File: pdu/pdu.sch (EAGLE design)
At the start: 18 parts, among them IC1 FDN359BN, IC2 FDN359BN, IC3 FDN359BN

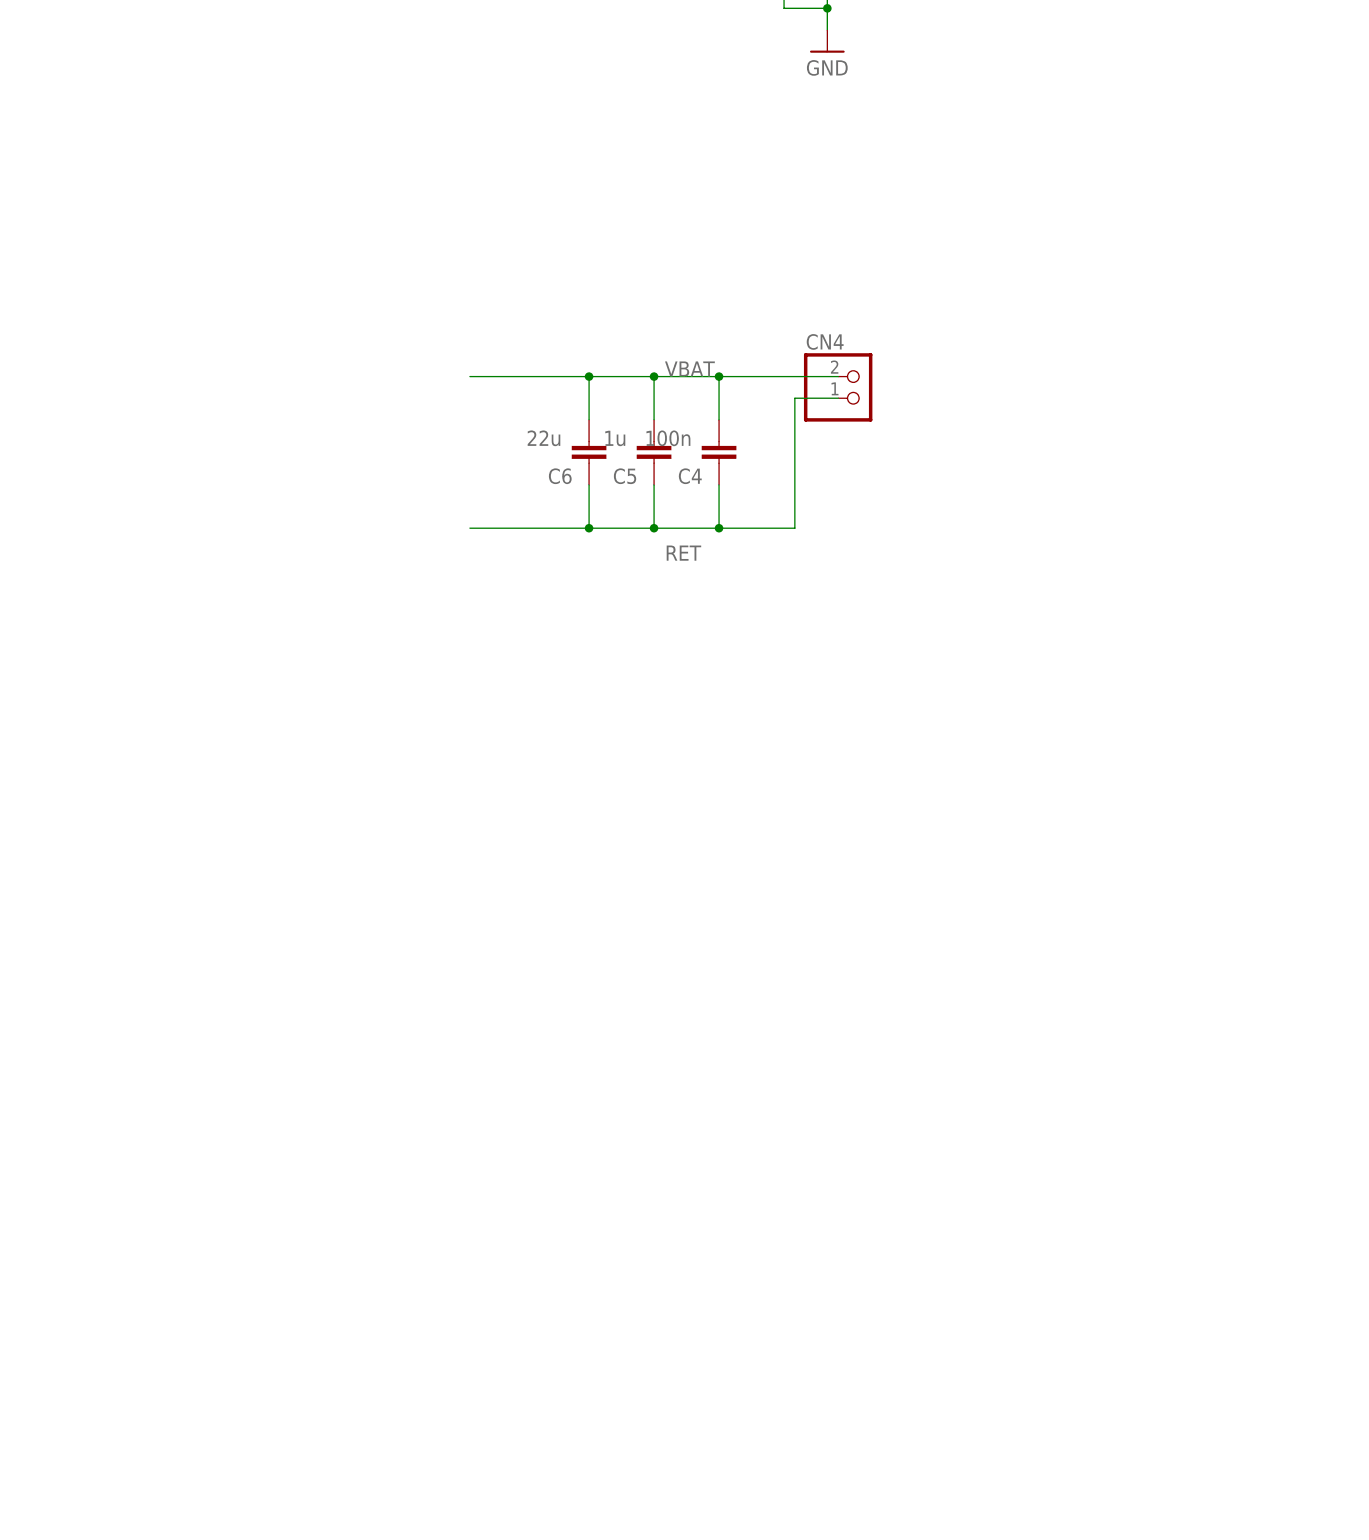
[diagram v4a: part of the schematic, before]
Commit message: fill length with conns
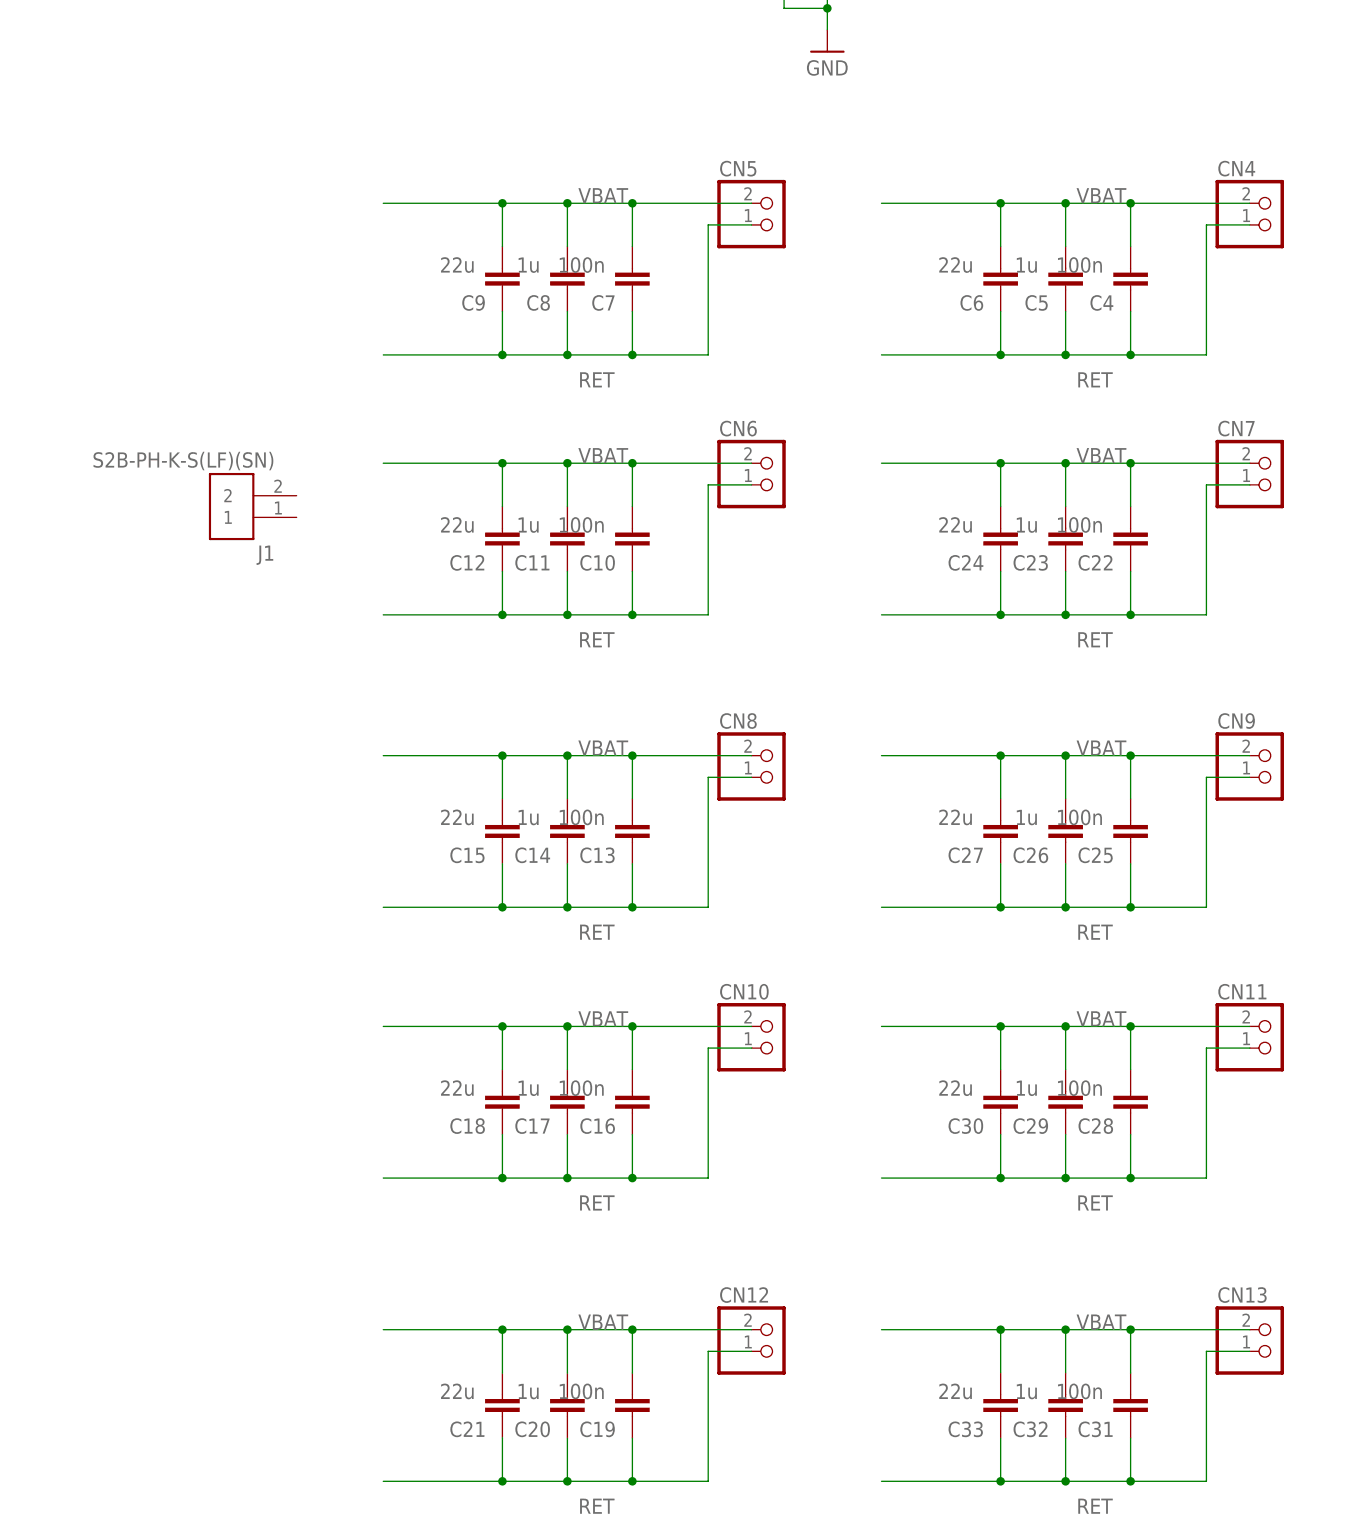
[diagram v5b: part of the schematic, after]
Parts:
- added C10, C13, C16, C19, C22, C25, C28, C31, C7: 100n, Capacitor:C_CHIP-0603(1608-METRIC)
- added C11, C14, C17, C20, C23, C26, C29, C32, C8: 1u, Capacitor:C_CHIP-0603(1608-METRIC)
- added C12, C15, C18, C21, C24, C27, C30, C33, C9: 22u, Capacitor:C_CHIP-0603(1608-METRIC)
- added CN10, CN11, CN12, CN13, CN5, CN6, CN7, CN8, CN9: (no value), adafruit:JST_2PIN-THM-RA
- added J1: S2B-PH-K-S(LF)(SN), Connectors:S2B-PH-K-S(LF)(SN)
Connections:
- net RET: now also C10.1, C11.1, C12.1, C13.1, C14.1, C15.1, C16.1, C17.1, C18.1, C19.1, C20.1, C21.1, C22.1, C23.1, C24.1, C25.1, C26.1, C27.1, C28.1, C29.1, C30.1, C31.1, C32.1, C33.1, C7.1, C8.1, C9.1, CN10.2, CN11.2, CN12.2, CN13.2, CN5.2, CN6.2, CN7.2, CN8.2, CN9.2
- net VBAT: now also C10.2, C11.2, C12.2, C13.2, C14.2, C15.2, C16.2, C17.2, C18.2, C19.2, C20.2, C21.2, C22.2, C23.2, C24.2, C25.2, C26.2, C27.2, C28.2, C29.2, C30.2, C31.2, C32.2, C33.2, C7.2, C8.2, C9.2, CN10.1, CN11.1, CN12.1, CN13.1, CN5.1, CN6.1, CN7.1, CN8.1, CN9.1
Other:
- moved on the sheet: C4, C5, C6, CN4

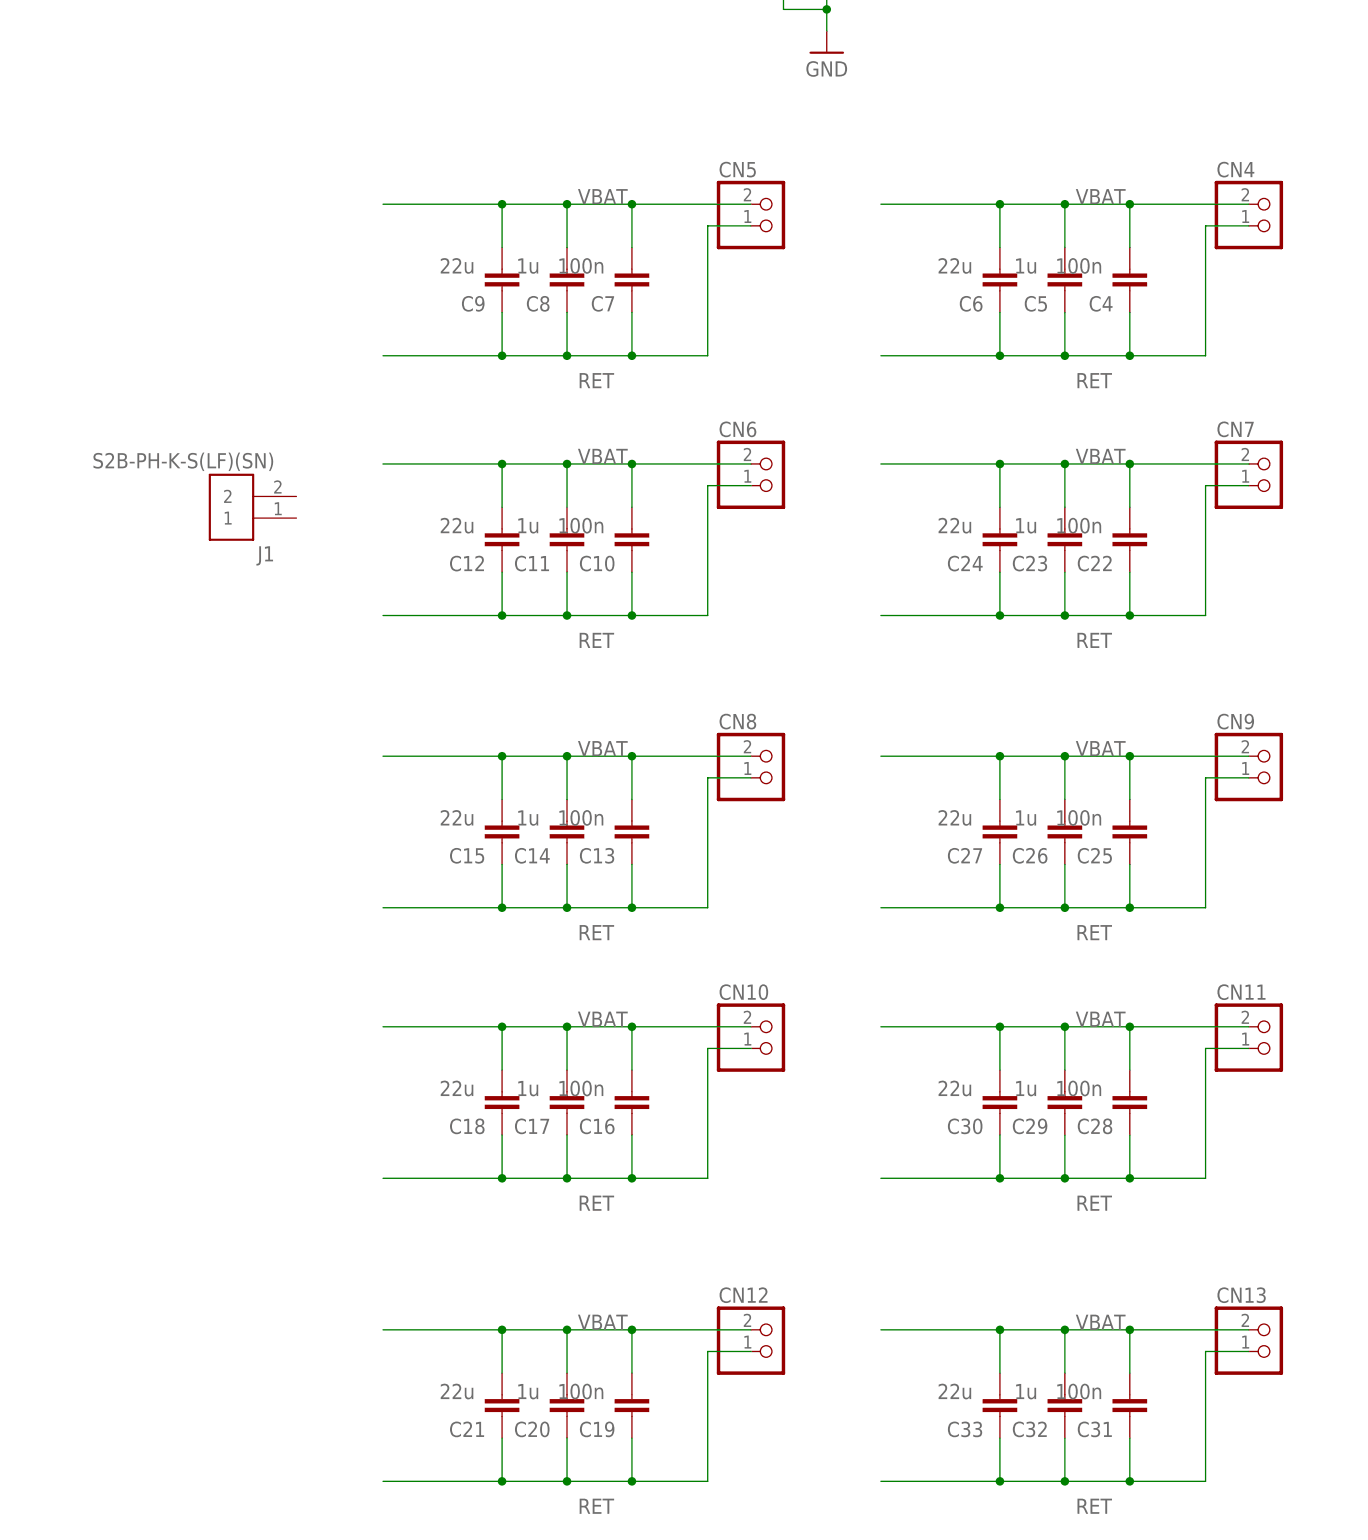
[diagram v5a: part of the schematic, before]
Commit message: swap connector
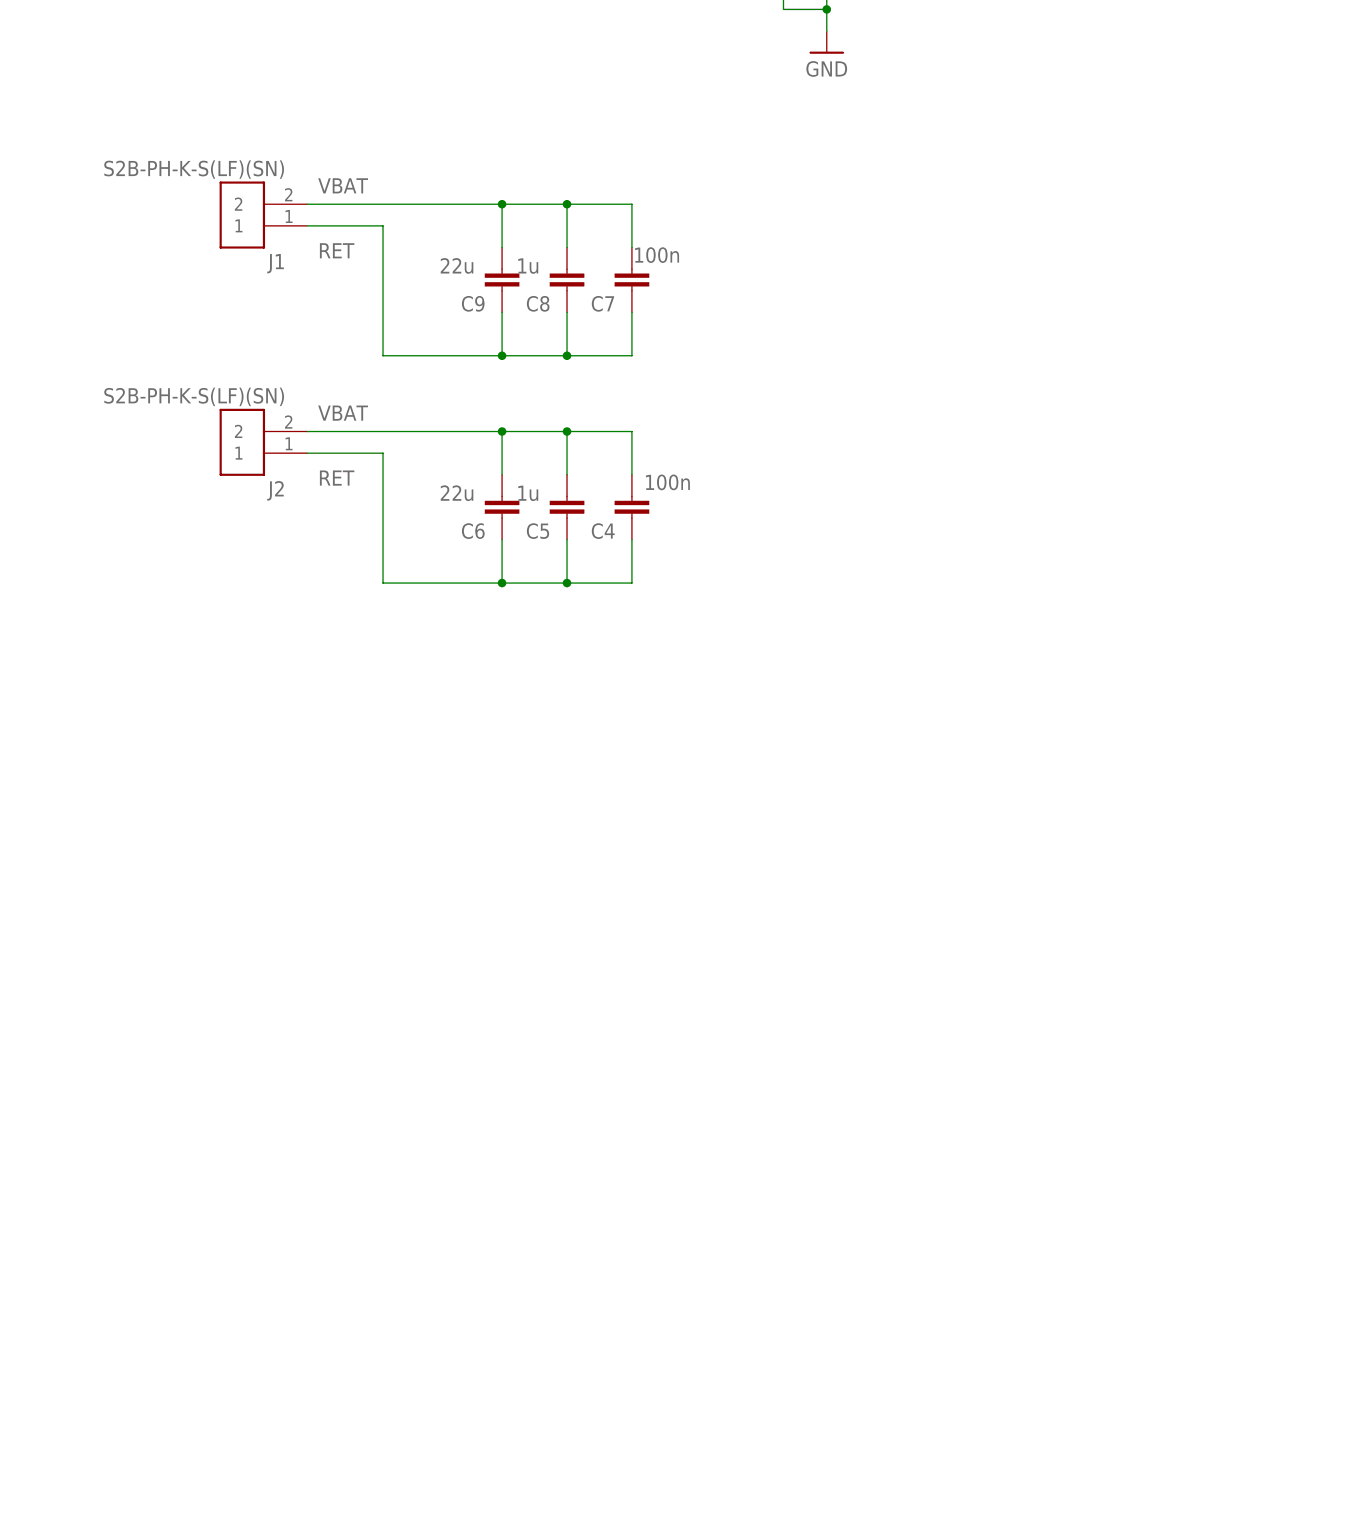
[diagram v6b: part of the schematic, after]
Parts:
- removed C10, C13, C16, C19, C22, C25, C28, C31: 100n, Capacitor:C_CHIP-0603(1608-METRIC)
- removed C11, C14, C17, C20, C23, C26, C29, C32: 1u, Capacitor:C_CHIP-0603(1608-METRIC)
- removed C12, C15, C18, C21, C24, C27, C30, C33: 22u, Capacitor:C_CHIP-0603(1608-METRIC)
- removed CN10, CN11, CN12, CN13, CN4, CN5, CN6, CN7, CN8, CN9: (no value), adafruit:JST_2PIN-THM-RA
- added J2: S2B-PH-K-S(LF)(SN), Connectors:S2B-PH-K-S(LF)(SN)
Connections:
- net RET: now also J1.1, J2.1; no longer C10.1, C11.1, C12.1, C13.1, C14.1, C15.1, C16.1, C17.1, C18.1, C19.1, C20.1, C21.1, C22.1, C23.1, C24.1, C25.1, C26.1, C27.1, C28.1, C29.1, C30.1, C31.1, C32.1, C33.1, CN10.2, CN11.2, CN12.2, CN13.2, CN4.2, CN5.2, CN6.2, CN7.2, CN8.2, CN9.2
- net VBAT: now also J1.2, J2.2; no longer C10.2, C11.2, C12.2, C13.2, C14.2, C15.2, C16.2, C17.2, C18.2, C19.2, C20.2, C21.2, C22.2, C23.2, C24.2, C25.2, C26.2, C27.2, C28.2, C29.2, C30.2, C31.2, C32.2, C33.2, CN10.1, CN11.1, CN12.1, CN13.1, CN4.1, CN5.1, CN6.1, CN7.1, CN8.1, CN9.1
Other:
- moved on the sheet: C4, C5, C6, J1

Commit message: fully populate board
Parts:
- added C10, C13, C16, C19, C22, C25, C28, C31: 100n, Capacitor:C_CHIP-0603(1608-METRIC)
- added C11, C14, C17, C20, C23, C26, C29, C32: 1u, Capacitor:C_CHIP-0603(1608-METRIC)
- added C12, C15, C18, C21, C24, C27, C30, C33: 22u, Capacitor:C_CHIP-0603(1608-METRIC)
- added J10, J3, J4, J5, J6, J7, J8, J9: S2B-PH-K-S(LF)(SN), Connectors:S2B-PH-K-S(LF)(SN)
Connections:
- net RET: now also C10.1, C11.1, C12.1, C13.1, C14.1, C15.1, C16.1, C17.1, C18.1, C19.1, C20.1, C21.1, C22.1, C23.1, C24.1, C25.1, C26.1, C27.1, C28.1, C29.1, C30.1, C31.1, C32.1, C33.1, J10.1, J3.1, J4.1, J5.1, J6.1, J7.1, J8.1, J9.1
- net VBAT: now also C10.2, C11.2, C12.2, C13.2, C14.2, C15.2, C16.2, C17.2, C18.2, C19.2, C20.2, C21.2, C22.2, C23.2, C24.2, C25.2, C26.2, C27.2, C28.2, C29.2, C30.2, C31.2, C32.2, C33.2, J10.2, J3.2, J4.2, J5.2, J6.2, J7.2, J8.2, J9.2
